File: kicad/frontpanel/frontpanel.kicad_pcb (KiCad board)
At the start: 2 copper layers, 91.4 x 128.5 mm, 2 parts

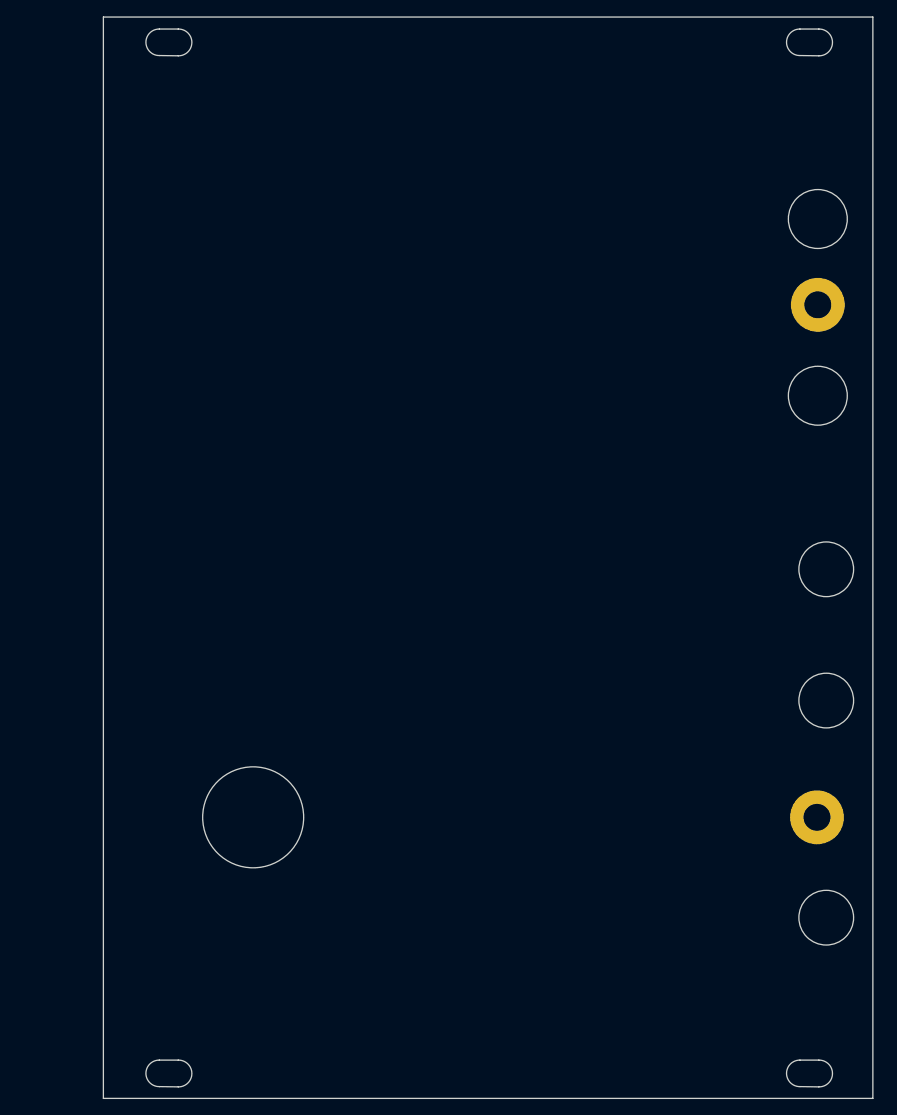
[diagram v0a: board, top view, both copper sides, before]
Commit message: front panel v1.0 to production
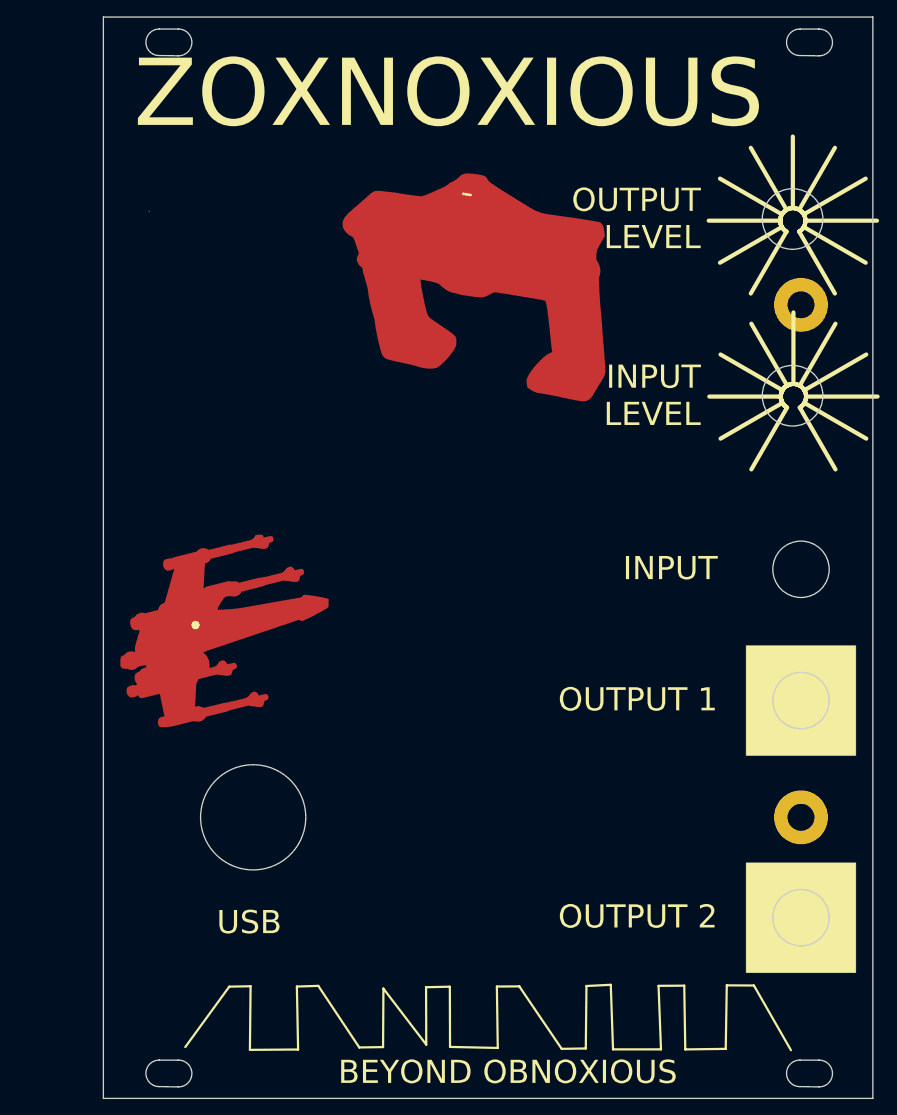
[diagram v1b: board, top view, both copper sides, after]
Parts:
- moved ? 2.00 mm to (167.3, 58.6)
- moved ? 1.90 mm to (167.3, 119.5)
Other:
- outline, holes or cut-outs redrawn
- board text added: "BEYOND OBNOXIOUS"
- board text added: "INPUT"
- board text added: "INPUT LEVEL"
- board text added: "OUTPUT 1"
- board text added: "OUTPUT 2"
- board text added: "OUTPUT LEVEL"
- board text added: "USB"
- board text added: "ZOXNOXIOUS"
